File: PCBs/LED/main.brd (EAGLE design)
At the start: 100 x 100 mm, 76 parts

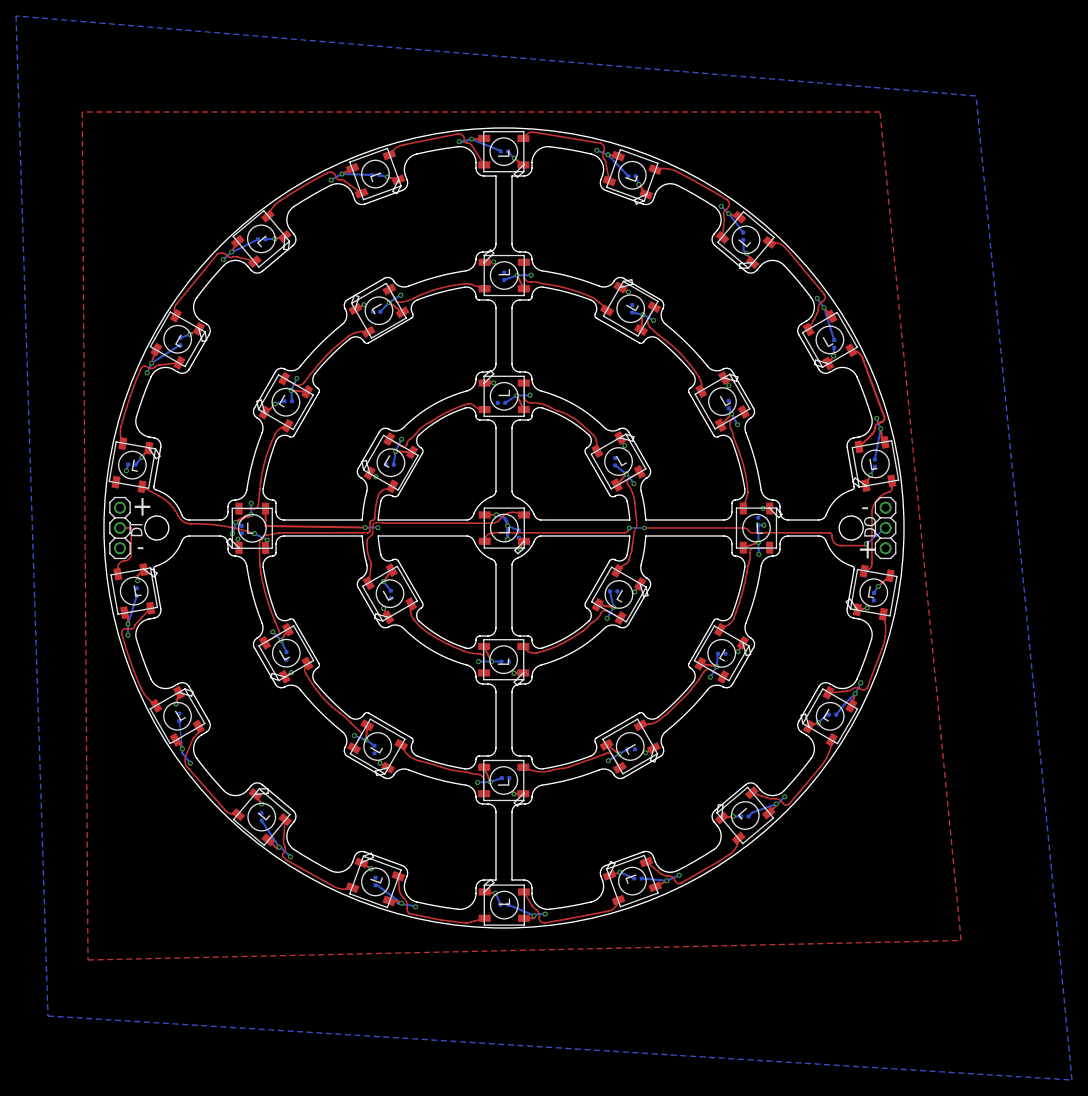
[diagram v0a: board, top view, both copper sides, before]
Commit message: changed size of capacitors from 0401 to 0805
(schematic not updated yet...)
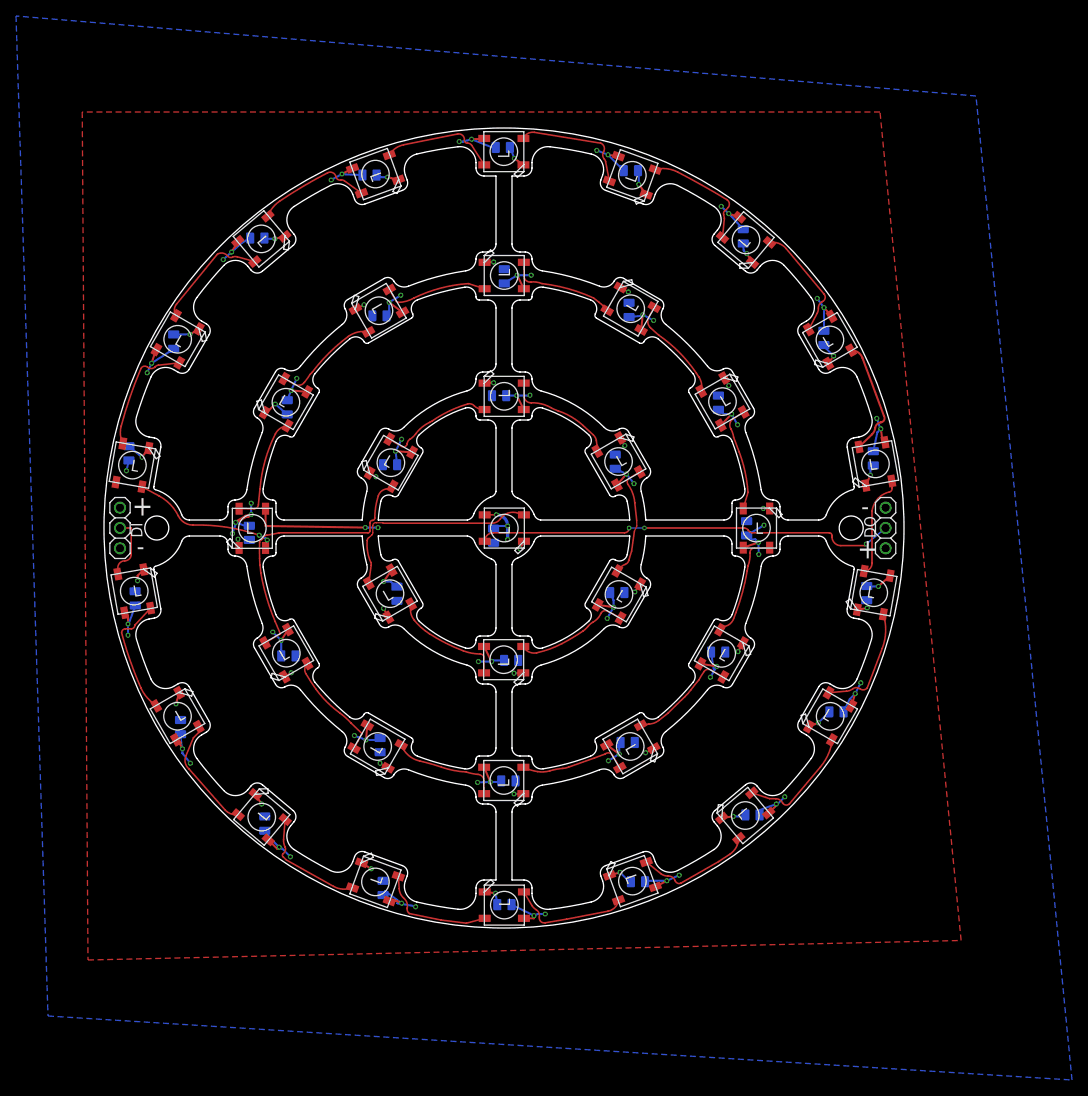
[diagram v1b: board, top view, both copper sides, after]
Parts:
- C1, C10, C11, C12, C13, C14, C15, C16, C17, C18, C19, C2, C20, C21, C22, C23, C24, C25, C26, C27, C28, C29, C3, C30, C31, C32, C33, C34, C35, C36, C37, C4, C5, C6, C7, C8, C9: device Seeed-Capacitor:C0402 -> OPL_Capacitor:C0805
- moved C2 3.16 mm to (-1.30, -0.96)
- moved C8 1.68 mm to (30.3, -0.03)
- moved C18 1.50 mm to (40.0, 23.8)
- moved C21 1.45 mm to (-46.9, 9.34), turned to 0 degrees
- moved C7 1.32 mm to (26.8, 15.7)
- moved C32 1.24 mm to (-15.1, -45.0)
- moved C33 1.21 mm to (-40.4, -24.9)
- moved C25 1.03 mm to (-31.8, -0.60)
- moved C16 1.01 mm to (45.3, -8.14)
- moved C12 0.97 mm to (31.1, -35.9)
- moved C36 0.96 mm to (15.5, -26.8)
- moved C37 0.95 mm to (-0.61, 16.5)
- moved C24 0.94 mm to (-29.9, -37.0)
- moved C15 0.89 mm to (-15.5, -27.1)
- moved C31 0.85 mm to (-41.3, 23.3)
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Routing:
- net VCC: track 230.0 -> 223.8 mm
- net GND: track 66.3 -> 71.9 mm
